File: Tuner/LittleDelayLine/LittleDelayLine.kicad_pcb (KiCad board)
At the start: 2 copper layers, 100 x 100 mm, 115 parts, among them J1 Conn_Coaxial, J10 Conn_Coaxial, J11 Conn_02x05_Odd_Even, J12 Conn_01x01, J13 Conn_01x01, J14 Conn_01x01, J15 Conn_01x01, J16 Conn_01x01, J17 Conn_Coaxial, J18 Conn_01x01, J19 Conn_01x01, J2 Conn_Coaxial, J20 Conn_01x01, J21 Conn_01x01, J22 Conn_Coaxial, J23 Conn_Coaxial, J24 Conn_Coaxial, J25 Conn_01x01, J26 Conn_01x01, J27 Conn_01x01, J28 Conn_01x01, J3 Conn_Coaxial, J4 Conn_Coaxial, J5 Conn_Coaxial, J6 Conn_Coaxial, J7 Conn_Coaxial, J8 Conn_Coaxial, J9 Conn_Coaxial, P10 Conn_01x01, P11 Conn_01x01, P12 Conn_01x01, P2 Conn_01x01, P3 Conn_01x01, P4 Conn_01x01, P5 Conn_01x01, P6 Conn_01x01, P7 Conn_01x01, P8 Conn_01x01, P9 Conn_01x01, U1 MCP23008, U2 ULN2803A

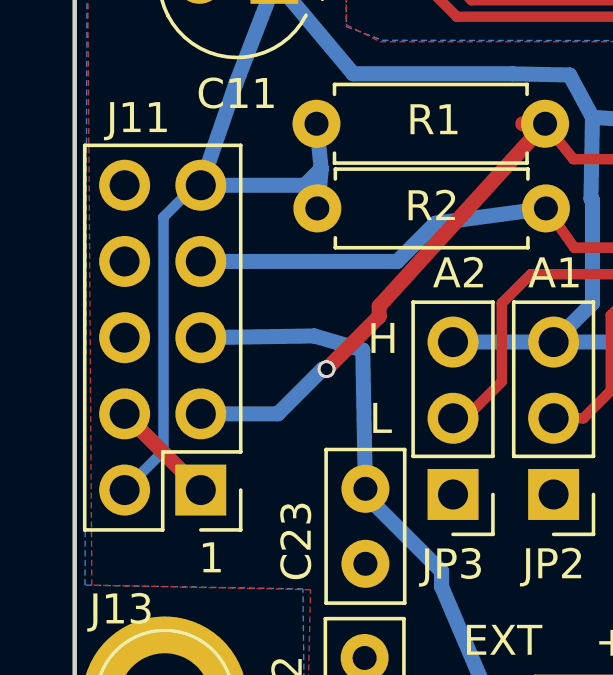
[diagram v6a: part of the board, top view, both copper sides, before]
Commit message: Changed I2C cable pinoutgit add Tunergit add Tuner Also added ICOM rig support
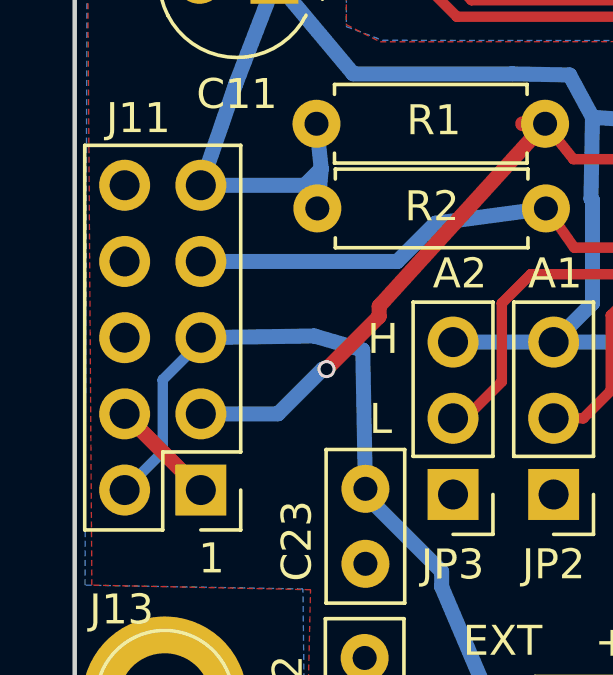
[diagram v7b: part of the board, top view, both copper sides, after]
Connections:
- J11 pad 2: +5V -> Net-(C23-Pad2)
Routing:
- net +5V: track 97.3 -> 85.7 mm
- net Net-(C23-Pad2): track 19.1 -> 25.9 mm
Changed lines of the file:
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@@
     (thickness 1.6)
     (drawings 41)
-    (tracks 741)
+    (tracks 743)
     (zones 0)
     (modules 115)
@@
   )
   (setup
-    (last_trace_width 1.5)
+    (last_trace_width 0.35)
     (user_trace_width 0.35)
     (user_trace_width 0.5)
@@
       (net 10 GND))
     (pad 2 thru_hole oval (at 2.54 0 180) (size 1.7 1.7) (drill 1) (layers *.Cu *.Mask)
-      (net 19 +5V))
+      (net 51 "Net-(C23-Pad2)"))
     (pad 3 thru_hole oval (at 0 2.54 180) (size 1.7 1.7) (drill 1) (layers *.Cu *.Mask)
       (net 52 SCL))
@@
   (segment (start 58.11266 130.62204) (end 58.08726 130.64744) (width 0.5) (layer B.Cu) (net 19) (status 30))
   (segment (start 54.2036 129.87528) (end 54.02072 129.87528) (width 0.35) (layer B.Cu) (net 19) (status 30))
-  (segment (start 54.02072 129.87528) (end 52.959 130.937) (width 0.35) (layer B.Cu) (net 19) (status 10))
-  (segment (start 52.959 138.73988) (end 51.6636 140.03528) (width 0.35) (layer B.Cu) (net 19) (status 20))
-  (segment (start 52.959 130.937) (end 52.959 138.73988) (width 0.35) (layer B.Cu) (net 19))
   (segment (start 73.025 140.462) (end 74.9554 140.462) (width 0.5) (layer B.Cu) (net 19) (status 10))
   (segment (start 75.04684 126.95936) (end 74.35088 126.2634) (width 0.5) (layer B.Cu) (net 19))
@@
   (segment (start 54.2036 129.87528) (end 55.372 126.492) (width 0.5) (layer B.Cu) (net 19) (status 10))
   (segment (start 55.372 126.492) (end 56.769 122.87504) (width 0.5) (layer B.Cu) (net 19) (status 20))
-  (segment (start 51.6636 140.03528) (end 51.6636 139.5603) (width 0.35) (layer B.Cu) (net 19) (status 30))
   (segment (start 56.769 122.87504) (end 56.769 123.12904) (width 1) (layer B.Cu) (net 19) (status 30))
   (segment (start 69.342 137.7188) (end 72.8218 137.7188) (width 0.35) (layer F.Cu) (net 20) (status 30))
@@
   (segment (start 146.0246 147.9804) (end 147.0025 147.0025) (width 1) (layer F.Cu) (net 50) (status 30))
   (segment (start 140.6652 147.9804) (end 140.6652 147.2184) (width 0.5) (layer F.Cu) (net 50) (status 30))
+  (segment (start 54.2036 134.95528) (end 54.2036 135.0899) (width 0.35) (layer B.Cu) (net 51))
+  (segment (start 54.2036 135.0899) (end 52.9336 136.3599) (width 0.35) (layer B.Cu) (net 51))
+  (segment (start 52.9336 138.76528) (end 51.6636 140.03528) (width 0.35) (layer B.Cu) (net 51))
+  (segment (start 52.9336 136.3599) (end 52.9336 138.76528) (width 0.35) (layer B.Cu) (net 51))
+  (segment (start 51.6636 140.03528) (end 51.87442 140.03528) (width 0.35) (layer B.Cu) (net 51))
+  (segment (start 51.6636 140.03528) (end 51.6636 139.5603) (width 0.35) (layer B.Cu) (net 51) (status 30))
   (segment (start 59.69 139.994) (end 59.69 140.208) (width 0.5) (layer B.Cu) (net 51) (status 30))
   (segment (start 59.69 140.208) (end 62.23 142.748) (width 0.5) (layer B.Cu) (net 51) (status 10))

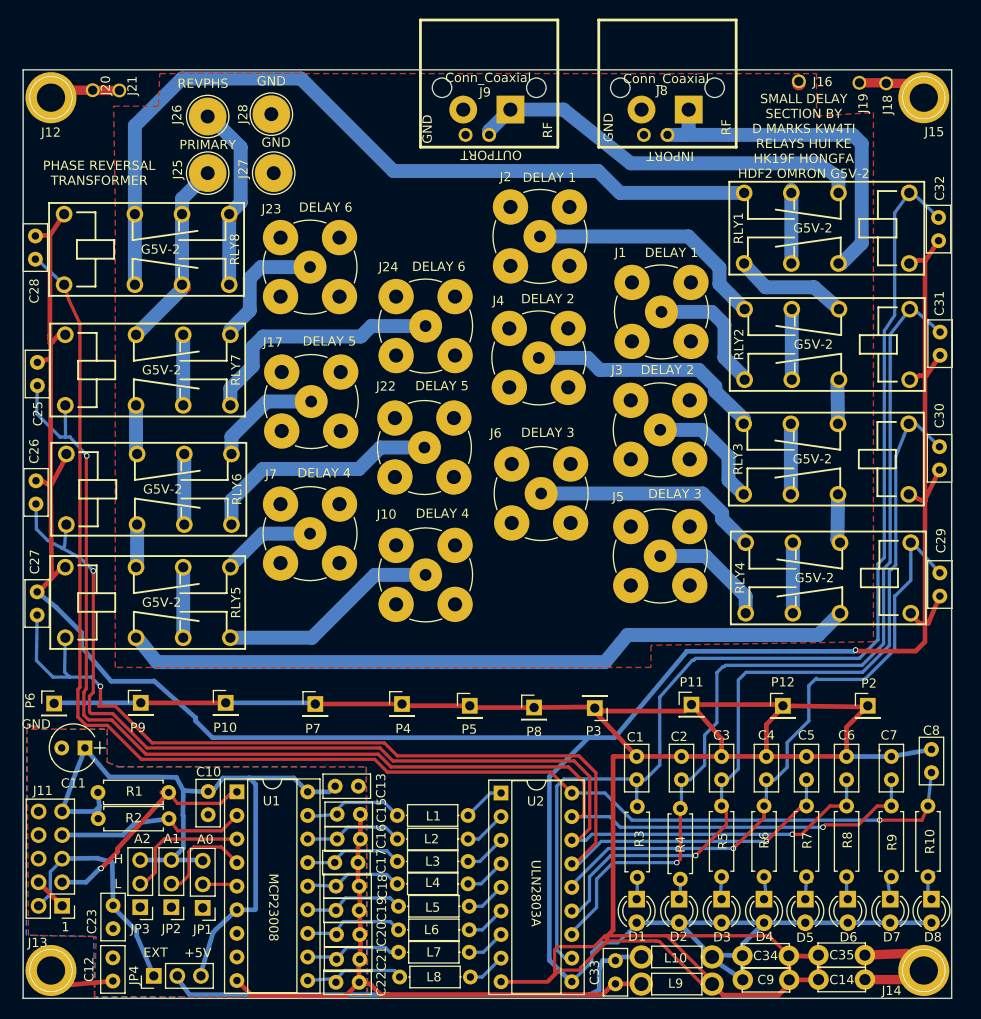
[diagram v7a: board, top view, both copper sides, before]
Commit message: Fixed icom tuning bad tuning report
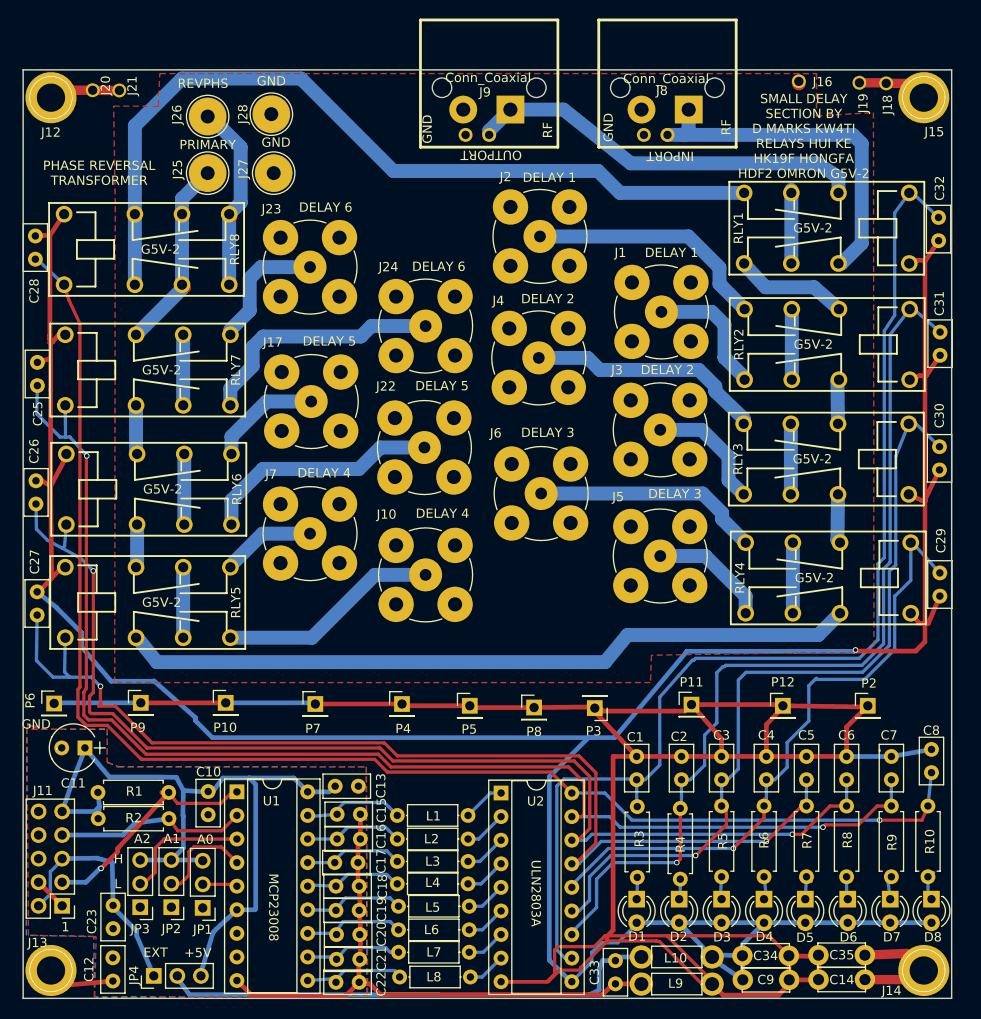
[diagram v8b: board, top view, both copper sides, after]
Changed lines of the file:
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@@
   )
   (setup
-    (last_trace_width 0.35)
+    (last_trace_width 0.25)
     (user_trace_width 0.35)
     (user_trace_width 0.5)
@@
     (polygon
       (pts
-        (xy 135.4455 54.9783) (xy 141.5796 54.5973) (xy 141.5796 111.5949) (xy 117.6147 111.9759) (xy 117.6147 114.3635)
-        (xy 59.9186 114.3635) (xy 59.9186 64.4525) (xy 59.75096 53.9115) (xy 64.55156 53.9115) (xy 64.7192 50.4063)
+        (xy 135.4455 54.9783) (xy 141.5796 54.5973) (xy 141.6304 112.6617) (xy 117.6655 113.0427) (xy 117.5639 115.9891)
+        (xy 59.8678 115.9891) (xy 59.9186 64.4525) (xy 59.75096 53.9115) (xy 64.55156 53.9115) (xy 64.7192 50.4063)
         (xy 135.4455 50.4063)
       )
